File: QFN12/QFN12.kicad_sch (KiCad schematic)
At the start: 5 parts, among them J1 Conn_01x06, J2 Conn_02x06_Counter_Clockwise, J3 Conn_01x06

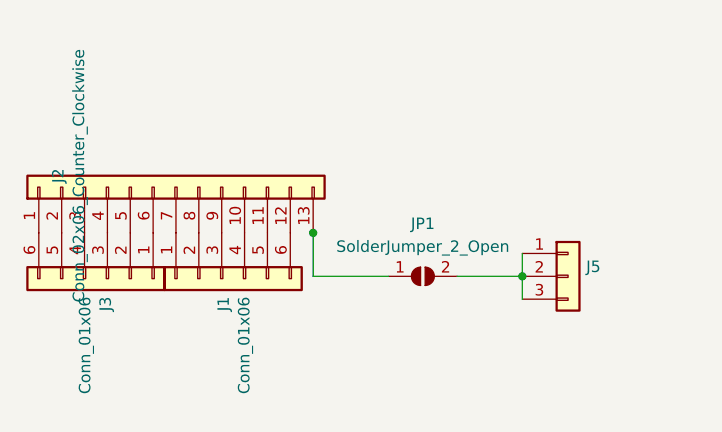
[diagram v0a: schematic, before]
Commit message: Add 722AG footpring on QFN12 backside
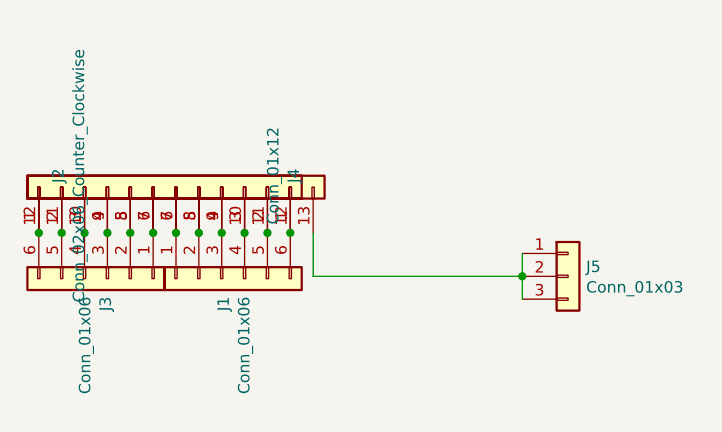
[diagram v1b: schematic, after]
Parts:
- removed JP1: SolderJumper_2_Open, Jumper:SolderJumper-2_P1.3mm_Open_TrianglePad1.0x1.5mm, symbol Jumper:SolderJumper_2_Open
- added J2: Conn_02x06_Counter_Clockwise, Package_DFN_QFN:QFN-12-1EP_3x3mm_P0.5mm_EP1.65x1.65mm, symbol Connector_Generic:Conn_01x13
- J4: renamed from J2; value Conn_02x06_Counter_Clockwise -> Conn_01x12; footprint Package_DFN_QFN:QFN-12-1EP_3x3mm_P0.5mm_EP1.65x1.65mm -> FUSB303TMX:QFN40P160X160X40-12N; symbol Connector_Generic:Conn_01x13 -> Connector_Generic:Conn_01x12
- J5: value (none) -> Conn_01x03; footprint (none) -> Connector_PinHeader_2.54mm:PinHeader_1x03_P2.54mm_Vertical
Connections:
- net at J3.1 (Pin_1): now also J4.7 (Pin_7), J2.6 (Pin_6); no longer J4.6 (Pin_6)
- net at J3.2 (Pin_2): now also J4.8 (Pin_8), J2.5 (Pin_5); no longer J4.5 (Pin_5)
- net at J3.3 (Pin_3): now also J4.9 (Pin_9), J2.4 (Pin_4); no longer J4.4 (Pin_4)
- net at J3.4 (Pin_4): now also J4.10 (Pin_10), J2.3 (Pin_3); no longer J4.3 (Pin_3)
- net at J3.5 (Pin_5): now also J4.11 (Pin_11), J2.2 (Pin_2); no longer J4.2 (Pin_2)
- net at J3.6 (Pin_6): now also J4.12 (Pin_12), J2.1 (Pin_1); no longer J4.1 (Pin_1)
- net at J1.4 (Pin_4): now also J4.3 (Pin_3), J2.10 (Pin_10); no longer J4.10 (Pin_10)
- net at J1.5 (Pin_5): now also J4.2 (Pin_2), J2.11 (Pin_11); no longer J4.11 (Pin_11)
- net at J1.6 (Pin_6): now also J4.1 (Pin_1), J2.12 (Pin_12); no longer J4.12 (Pin_12)
- net at J1.1 (Pin_1): now also J4.6 (Pin_6), J2.7 (Pin_7); no longer J4.7 (Pin_7)
- net at J1.2 (Pin_2): now also J4.5 (Pin_5), J2.8 (Pin_8); no longer J4.8 (Pin_8)
- net at J1.3 (Pin_3): now also J4.4 (Pin_4), J2.9 (Pin_9); no longer J4.9 (Pin_9)
- net at J5.1 (Pin_1), J5.2 (Pin_2), J5.3 (Pin_3): now also J2.13 (Pin_13)
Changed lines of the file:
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@@
     (comment 3 "DIP16 P = 2.54mm")
+  )
+  (junction (at 73.152 36.957) (diameter 0) (color 0 0 0 0)
+  )
+  (junction (at 50.292 36.957) (diameter 0) (color 0 0 0 0)
+  )
+  (junction (at 70.612 36.957) (diameter 0) (color 0 0 0 0)
+  )
+  (junction (at 47.752 36.957) (diameter 0) (color 0 0 0 0)
+  )
+  (junction (at 60.452 36.957) (diameter 0) (color 0 0 0 0)
+  )
+  (junction (at 57.912 36.957) (diameter 0) (color 0 0 0 0)
+  )
+  (junction (at 62.992 36.957) (diameter 0) (color 0 0 0 0)
+  )
+  (junction (at 52.832 36.957) (diameter 0) (color 0 0 0 0)
+  )
+  (junction (at 45.212 36.957) (diameter 0) (color 0 0 0 0)
+  )
+  (junction (at 55.372 36.957) (diameter 0) (color 0 0 0 0)
   )
   (junction (at 98.933 41.783) (diameter 0) (color 0 0 0 0)
   )
-  (junction (at 75.692 36.957) (diameter 0) (color 0 0 0 0)
+  (junction (at 68.072 36.957) (diameter 0) (color 0 0 0 0)
+  )
+  (junction (at 65.532 36.957) (diameter 0) (color 0 0 0 0)
   )
   (wire (pts (xy 98.933 39.243) (xy 98.933 41.783))
     (stroke (width 0) (type default) (color 0 0 0 0))
   )
-  (wire (pts (xy 91.694 41.783) (xy 98.933 41.783))
-    (stroke (width 0) (type default) (color 0 0 0 0))
-  )
-  (wire (pts (xy 75.692 36.83) (xy 75.692 36.957))
-    (stroke (width 0) (type default) (color 0 0 0 0))
-  )
-  (wire (pts (xy 75.692 41.783) (xy 84.074 41.783))
+  (wire (pts (xy 75.692 41.783) (xy 98.933 41.783))
     (stroke (width 0) (type default) (color 0 0 0 0))
   )
@@
     (pin "6")
   )
-  (symbol (lib_id "Connector_Generic:Conn_01x13") (at 60.452 31.877 90) (unit 1)
+  (symbol (lib_id "Connector_Generic:Conn_01x12") (at 60.452 31.877 270) (mirror x) (unit 1)
     (in_bom yes) (on_board yes)
-    (property "Reference" "J2" (id 0) (at 47.371 30.607 0))
-    (property "Value" "Conn_02x06_Counter_Clockwise" (id 1) (at 49.657 30.607 0))
-    (property "Footprint" "Package_DFN_QFN:QFN-12-1EP_3x3mm_P0.5mm_EP1.65x1.65mm" (id 2) (at 60.452 31.877 0)
+    (property "Reference" "J4" (id 0) (at 73.533 30.607 0))
+    (property "Value" "Conn_01x12" (id 1) (at 71.247 30.607 0))
+    (property "Footprint" "FUSB303TMX:QFN40P160X160X40-12N" (id 2) (at 60.452 31.877 0)
       (effects (font (size 1.27 1.27)) hide)
     )
@@
     (pin "11")
     (pin "12")
-    (pin "13")
     (pin "2")
     (pin "3")
@@
       (effects (font (size 1.27 1.27)) (justify left))
     )
-    (property "Value" "" (id 1) (at 106.0196 43.0022 0)
+    (property "Value" "Conn_01x03" (id 1) (at 106.0196 43.0022 0)
       (effects (font (size 1.27 1.27)) (justify left))
     )
-    (property "Footprint" "" (id 2) (at 104.013 41.783 0)
+    (property "Footprint" "Connector_PinHeader_2.54mm:PinHeader_1x03_P2.54mm_Vertical" (id 2) (at 104.013 41.783 0)
       (effects (font (size 1.27 1.27)) hide)
     )
@@
     (pin "3")
   )
-  (symbol (lib_id "Jumper:SolderJumper_2_Open") (at 87.884 41.783 0) (unit 1)
-    (in_bom yes) (on_board yes) (fields_autoplaced)
-    (property "Reference" "JP1" (id 0) (at 87.884 35.941 0))
-    (property "Value" "SolderJumper_2_Open" (id 1) (at 87.884 38.481 0))
-    (property "Footprint" "Jumper:SolderJumper-2_P1.3mm_Open_TrianglePad1.0x1.5mm" (id 2) (at 87.884 41.783 0)
+  (symbol (lib_id "Connector_Generic:Conn_01x13") (at 60.452 31.877 90) (unit 1)
+    (in_bom yes) (on_board yes)
+    (property "Reference" "J2" (id 0) (at 47.371 30.607 0))
+    (property "Value" "Conn_02x06_Counter_Clockwise" (id 1) (at 49.657 30.607 0))
+    (property "Footprint" "Package_DFN_QFN:QFN-12-1EP_3x3mm_P0.5mm_EP1.65x1.65mm" (id 2) (at 60.452 31.877 0)
       (effects (font (size 1.27 1.27)) hide)
     )
-    (property "Datasheet" "~" (id 3) (at 87.884 41.783 0)
+    (property "Datasheet" "~" (id 3) (at 60.452 31.877 0)
       (effects (font (size 1.27 1.27)) hide)
     )
     (pin "1")
+    (pin "10")
+    (pin "11")
+    (pin "12")
+    (pin "13")
     (pin "2")
+    (pin "3")
+    (pin "4")
+    (pin "5")
+    (pin "6")
+    (pin "7")
+    (pin "8")
+    (pin "9")
   )
   (sheet_instances
@@
       (reference "J1") (unit 1) (value "Conn_01x06") (footprint "Connector_PinHeader_2.54mm:PinHeader_1x06_P2.54mm_Vertical")
     )
-    (path "/00000000-0000-0000-0000-00005d2772f5"
+    (path "/cfdaf3cf-9d92-43e9-8891-9b5dbff0c569"
       (reference "J2") (unit 1) (value "Conn_02x06_Counter_Clockwise") (footprint "Package_DFN_QFN:QFN-12-1EP_3x3mm_P0.5mm_EP1.65x1.65mm")
     )
@@
       (reference "J3") (unit 1) (value "Conn_01x06") (footprint "Connector_PinHeader_2.54mm:PinHeader_1x06_P2.54mm_Vertical")
     )
+    (path "/00000000-0000-0000-0000-00005d2772f5"
+      (reference "J4") (unit 1) (value "Conn_01x12") (footprint "FUSB303TMX:QFN40P160X160X40-12N")
+    )
     (path "/00000000-0000-0000-0000-00005d3b084d"
       (reference "J5") (unit 1) (value "Conn_01x03") (footprint "Connector_PinHeader_2.54mm:PinHeader_1x03_P2.54mm_Vertical")
     )
-    (path "/39b73c9c-39d7-491b-9834-76ba320a4f4c"
-      (reference "JP1") (unit 1) (value "SolderJumper_2_Open") (footprint "Jumper:SolderJumper-2_P1.3mm_Open_TrianglePad1.0x1.5mm")
-    )
   )
